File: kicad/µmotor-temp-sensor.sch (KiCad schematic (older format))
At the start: 0 parts

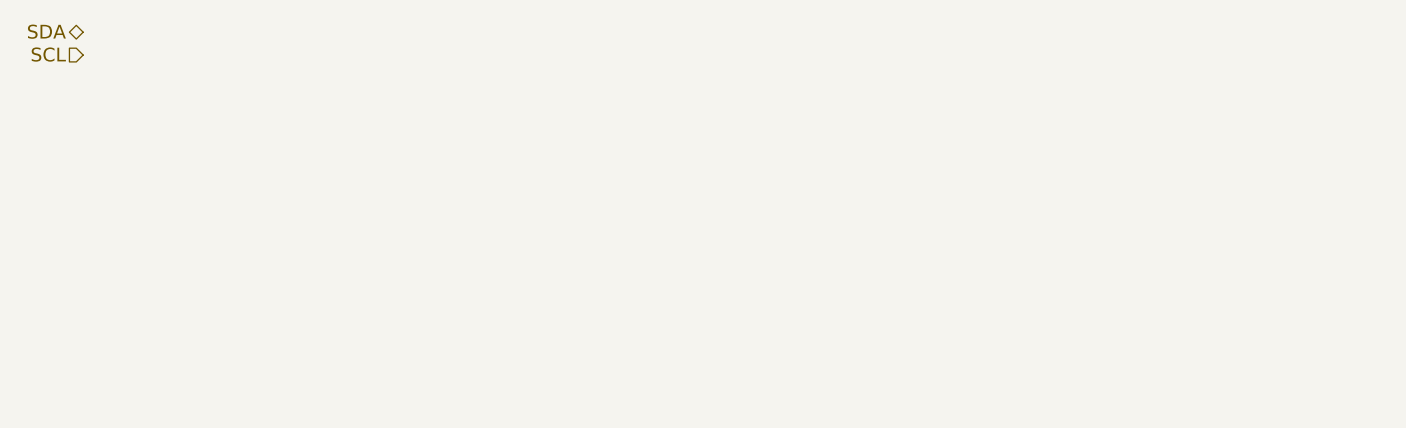
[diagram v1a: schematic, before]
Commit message: update µC pinout, motor driver, CubeMX, add 3V3 regulator and temperature sensor
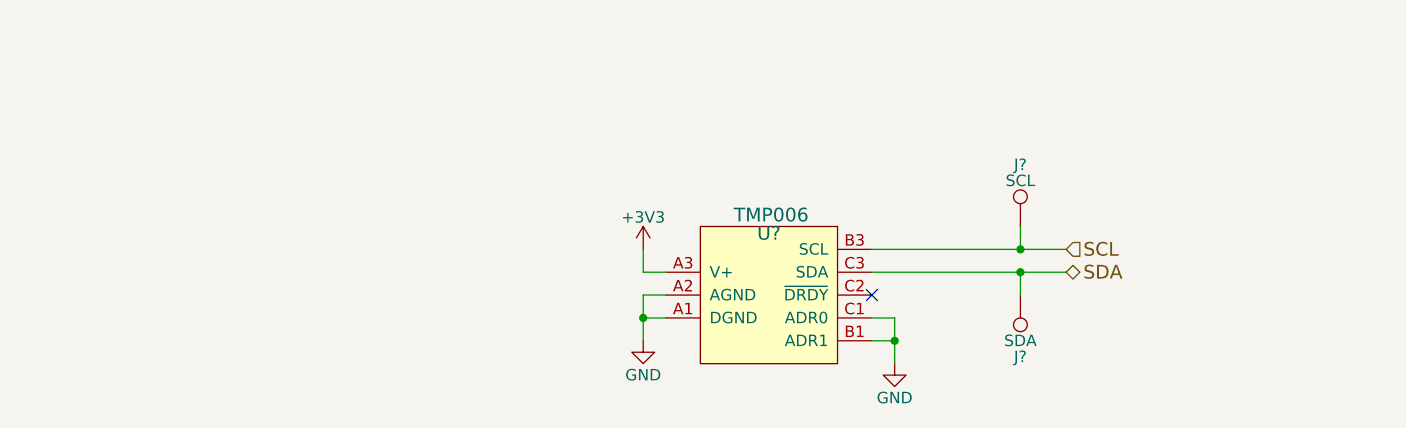
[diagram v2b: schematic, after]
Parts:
- added J?: SCL, symbol TEST_1P
- added J?: SDA, symbol TEST_1P
- added U?: TMP006, symbol TMP006
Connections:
- net SCL: now also J?.1, U?.B3 (SCL)
- net SDA: now also J?.1, U?.C3 (SDA)
- new net +3V3: U?.A3 (V+)
- new net GND: U?.A1 (DGND), U?.A2 (AGND), U?.B1 (ADR1), U?.C1 (ADR0)
- no-connect marks 0 -> 1
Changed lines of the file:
@@
 LIBS:drv8323s
 LIBS:FDMD82xx
+LIBS:ncp4623
+LIBS:TMP006
 LIBS:µmotor-cache
 EELAYER 25 0
@@
 $Descr A4 11693 8268
 encoding utf-8
-Sheet 7 6
+Sheet 6 6
 Title "µmotor - Micro Motor Controller"
 Date "2017-09-14"
@@
 Comment4 ""
 $EndDescr
-Text HLabel 1100 1050 0    60   BiDi ~ 0
+Text HLabel 5400 2100 2    60   BiDi ~ 0
 SDA
-Text HLabel 1100 1150 0    60   Input ~ 0
+Text HLabel 5400 2000 2    60   Input ~ 0
 SCL
+$Comp
+L TMP006 U?
+U 1 1 5A76B190
+P 4100 2200
+F 0 "U?" H 4100 2470 60  0000 C CNN
+F 1 "TMP006" H 4110 2550 60  0000 C CNN
+F 2 "" H 4100 2200 60  0001 C CNN
+F 3 "" H 4100 2200 60  0001 C CNN
+	1    4100 2200
+	1    0    0    -1
+$EndComp
+NoConn ~ 4550 2200
+$Comp
+L GND #PWR?
+U 1 1 5A76B49A
+P 4650 2500
+F 0 "#PWR?" H 4650 2250 50  0001 C CNN
+F 1 "GND" H 4650 2350 50  0000 C CNN
+F 2 "" H 4650 2500 50  0001 C CNN
+F 3 "" H 4650 2500 50  0001 C CNN
+	1    4650 2500
+	1    0    0    -1
+$EndComp
+Wire Wire Line
+	4650 2300 4650 2500
+Wire Wire Line
+	4650 2400 4550 2400
+Wire Wire Line
+	4650 2300 4550 2300
+Connection ~ 4650 2400
+$Comp
+L GND #PWR?
+U 1 1 5A76B4B9
+P 3550 2400
+F 0 "#PWR?" H 3550 2150 50  0001 C CNN
+F 1 "GND" H 3550 2250 50  0000 C CNN
+F 2 "" H 3550 2400 50  0001 C CNN
+F 3 "" H 3550 2400 50  0001 C CNN
+	1    3550 2400
+	1    0    0    -1
+$EndComp
+Wire Wire Line
+	3550 2200 3550 2400
+Wire Wire Line
+	3550 2300 3650 2300
+Wire Wire Line
+	3650 2200 3550 2200
+Connection ~ 3550 2300
+$Comp
+L +3V3 #PWR?
+U 1 1 5A76B4E0
+P 3550 2000
+F 0 "#PWR?" H 3550 1850 50  0001 C CNN
+F 1 "+3V3" H 3550 2140 50  0000 C CNN
+F 2 "" H 3550 2000 50  0001 C CNN
+F 3 "" H 3550 2000 50  0001 C CNN
+	1    3550 2000
+	1    0    0    -1
+$EndComp
+Wire Wire Line
+	3550 2000 3550 2100
+Wire Wire Line
+	3550 2100 3650 2100
+Wire Wire Line
+	4550 2000 5400 2000
+Wire Wire Line
+	4550 2100 5400 2100
+$Comp
+L TEST_1P J?
+U 1 1 5A76B941
+P 5200 1900
+F 0 "J?" H 5200 2170 50  0000 C CNN
+F 1 "SCL" H 5200 2100 50  0000 C CNN
+F 2 "" H 5400 1900 50  0001 C CNN
+F 3 "" H 5400 1900 50  0001 C CNN
+	1    5200 1900
+	1    0    0    -1
+$EndComp
+$Comp
+L TEST_1P J?
+U 1 1 5A76B97E
+P 5200 2200
+F 0 "J?" H 5200 2470 50  0000 C CNN
+F 1 "SDA" H 5200 2400 50  0000 C CNN
+F 2 "" H 5400 2200 50  0001 C CNN
+F 3 "" H 5400 2200 50  0001 C CNN
+	1    5200 2200
+	-1   0    0    1
+$EndComp
+Wire Wire Line
+	5200 2200 5200 2100
+Connection ~ 5200 2100
+Wire Wire Line
+	5200 2000 5200 1900
+Connection ~ 5200 2000
 $EndSCHEMATC

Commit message: layout: components placed
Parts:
- added J503: 3V3, Measurement_Point_Round-SMD-Pad_Smaller:Measurement_Point_Round-SMD-Pad_Smaller_0.75mm, symbol TEST_1P
- added J504: GND, Measurement_Point_Round-SMD-Pad_Smaller:Measurement_Point_Round-SMD-Pad_Smaller_0.75mm, symbol TEST_1P
- J501, J502: renamed from J?; footprint (none) -> Measurement_Point_Round-SMD-Pad_Smaller:Measurement_Point_Round-SMD-Pad_Smaller_0.75mm
- U501: renamed from U?; footprint (none) -> WCSP-8_1.6x1.6mm_P0.5mm:WCSP-8_1.6x1.6mm_P0.5mm
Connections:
- net +3V3: now also J503.1
- net GND: now also J504.1
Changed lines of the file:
@@
 LIBS:conn
 LIBS:linear
-LIBS:regul
-LIBS:74xx
-LIBS:cmos4000
-LIBS:adc-dac
-LIBS:memory
-LIBS:xilinx
-LIBS:microcontrollers
-LIBS:dsp
-LIBS:microchip
-LIBS:analog_switches
-LIBS:motorola
 LIBS:texas
-LIBS:intel
-LIBS:audio
 LIBS:interface
-LIBS:digital-audio
-LIBS:philips
-LIBS:display
-LIBS:cypress
-LIBS:siliconi
-LIBS:opto
-LIBS:atmel
 LIBS:contrib
 LIBS:valves
-LIBS:stm32
 LIBS:DRV8870
 LIBS:INA180A
@@
 LIBS:ncp4623
 LIBS:TMP006
+LIBS:stm32
 LIBS:µmotor-cache
 EELAYER 25 0
@@
 SCL
 $Comp
-L TMP006 U?
+L TMP006 U501
 U 1 1 5A76B190
 P 4100 2200
-F 0 "U?" H 4100 2470 60  0000 C CNN
+F 0 "U501" H 4100 2470 60  0000 C CNN
 F 1 "TMP006" H 4110 2550 60  0000 C CNN
-F 2 "" H 4100 2200 60  0001 C CNN
+F 2 "WCSP-8_1.6x1.6mm_P0.5mm:WCSP-8_1.6x1.6mm_P0.5mm" H 4100 2200 60  0001 C CNN
 F 3 "" H 4100 2200 60  0001 C CNN
 	1    4100 2200
@@
 NoConn ~ 4550 2200
 $Comp
-L GND #PWR?
+L GND #PWR026
 U 1 1 5A76B49A
 P 4650 2500
-F 0 "#PWR?" H 4650 2250 50  0001 C CNN
+F 0 "#PWR026" H 4650 2250 50  0001 C CNN
 F 1 "GND" H 4650 2350 50  0000 C CNN
 F 2 "" H 4650 2500 50  0001 C CNN
@@
 Connection ~ 4650 2400
 $Comp
-L GND #PWR?
+L GND #PWR027
 U 1 1 5A76B4B9
 P 3550 2400
-F 0 "#PWR?" H 3550 2150 50  0001 C CNN
+F 0 "#PWR027" H 3550 2150 50  0001 C CNN
 F 1 "GND" H 3550 2250 50  0000 C CNN
 F 2 "" H 3550 2400 50  0001 C CNN
@@
 Connection ~ 3550 2300
 $Comp
-L +3V3 #PWR?
+L +3V3 #PWR028
 U 1 1 5A76B4E0
 P 3550 2000
-F 0 "#PWR?" H 3550 1850 50  0001 C CNN
+F 0 "#PWR028" H 3550 1850 50  0001 C CNN
 F 1 "+3V3" H 3550 2140 50  0000 C CNN
 F 2 "" H 3550 2000 50  0001 C CNN
@@
 	4550 2100 5400 2100
 $Comp
-L TEST_1P J?
+L TEST_1P J501
 U 1 1 5A76B941
 P 5200 1900
-F 0 "J?" H 5200 2170 50  0000 C CNN
+F 0 "J501" H 5200 2170 50  0000 C CNN
 F 1 "SCL" H 5200 2100 50  0000 C CNN
-F 2 "" H 5400 1900 50  0001 C CNN
+F 2 "Measurement_Point_Round-SMD-Pad_Smaller:Measurement_Point_Round-SMD-Pad_Smaller_0.75mm" H 5400 1900 50  0001 C CNN
 F 3 "" H 5400 1900 50  0001 C CNN
 	1    5200 1900
@@
 $EndComp
 $Comp
-L TEST_1P J?
+L TEST_1P J502
 U 1 1 5A76B97E
 P 5200 2200
-F 0 "J?" H 5200 2470 50  0000 C CNN
+F 0 "J502" H 5200 2470 50  0000 C CNN
 F 1 "SDA" H 5200 2400 50  0000 C CNN
-F 2 "" H 5400 2200 50  0001 C CNN
+F 2 "Measurement_Point_Round-SMD-Pad_Smaller:Measurement_Point_Round-SMD-Pad_Smaller_0.75mm" H 5400 2200 50  0001 C CNN
 F 3 "" H 5400 2200 50  0001 C CNN
 	1    5200 2200
@@
 	5200 2000 5200 1900
 Connection ~ 5200 2000
+$Comp
+L TEST_1P J503
+U 1 1 5A77F3B3
+P 6450 2100
+F 0 "J503" H 6450 2370 50  0000 C CNN
+F 1 "3V3" H 6450 2300 50  0000 C CNN
+F 2 "Measurement_Point_Round-SMD-Pad_Smaller:Measurement_Point_Round-SMD-Pad_Smaller_0.75mm" H 6650 2100 50  0001 C CNN
+F 3 "" H 6650 2100 50  0001 C CNN
+	1    6450 2100
+	1    0    0    -1
+$EndComp
+$Comp
+L TEST_1P J504
+U 1 1 5A77F3FB
+P 6700 2100
+F 0 "J504" H 6700 2370 50  0000 C CNN
+F 1 "GND" H 6700 2300 50  0000 C CNN
+F 2 "Measurement_Point_Round-SMD-Pad_Smaller:Measurement_Point_Round-SMD-Pad_Smaller_0.75mm" H 6900 2100 50  0001 C CNN
+F 3 "" H 6900 2100 50  0001 C CNN
+	1    6700 2100
+	1    0    0    -1
+$EndComp
+$Comp
+L GND #PWR029
+U 1 1 5A77F465
+P 6700 2200
+F 0 "#PWR029" H 6700 1950 50  0001 C CNN
+F 1 "GND" H 6700 2050 50  0000 C CNN
+F 2 "" H 6700 2200 50  0001 C CNN
+F 3 "" H 6700 2200 50  0001 C CNN
+	1    6700 2200
+	1    0    0    -1
+$EndComp
+Wire Wire Line
+	6700 2200 6700 2100
+$Comp
+L +3V3 #PWR030
+U 1 1 5A77F497
+P 6450 2200
+F 0 "#PWR030" H 6450 2050 50  0001 C CNN
+F 1 "+3V3" H 6450 2340 50  0000 C CNN
+F 2 "" H 6450 2200 50  0001 C CNN
+F 3 "" H 6450 2200 50  0001 C CNN
+	1    6450 2200
+	-1   0    0    1
+$EndComp
+Wire Wire Line
+	6450 2200 6450 2100
 $EndSCHEMATC
